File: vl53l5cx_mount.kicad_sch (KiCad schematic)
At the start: 10 parts, among them J1 Conn_01x05_MountingPin, U1 VL53L5CXV0GC/1

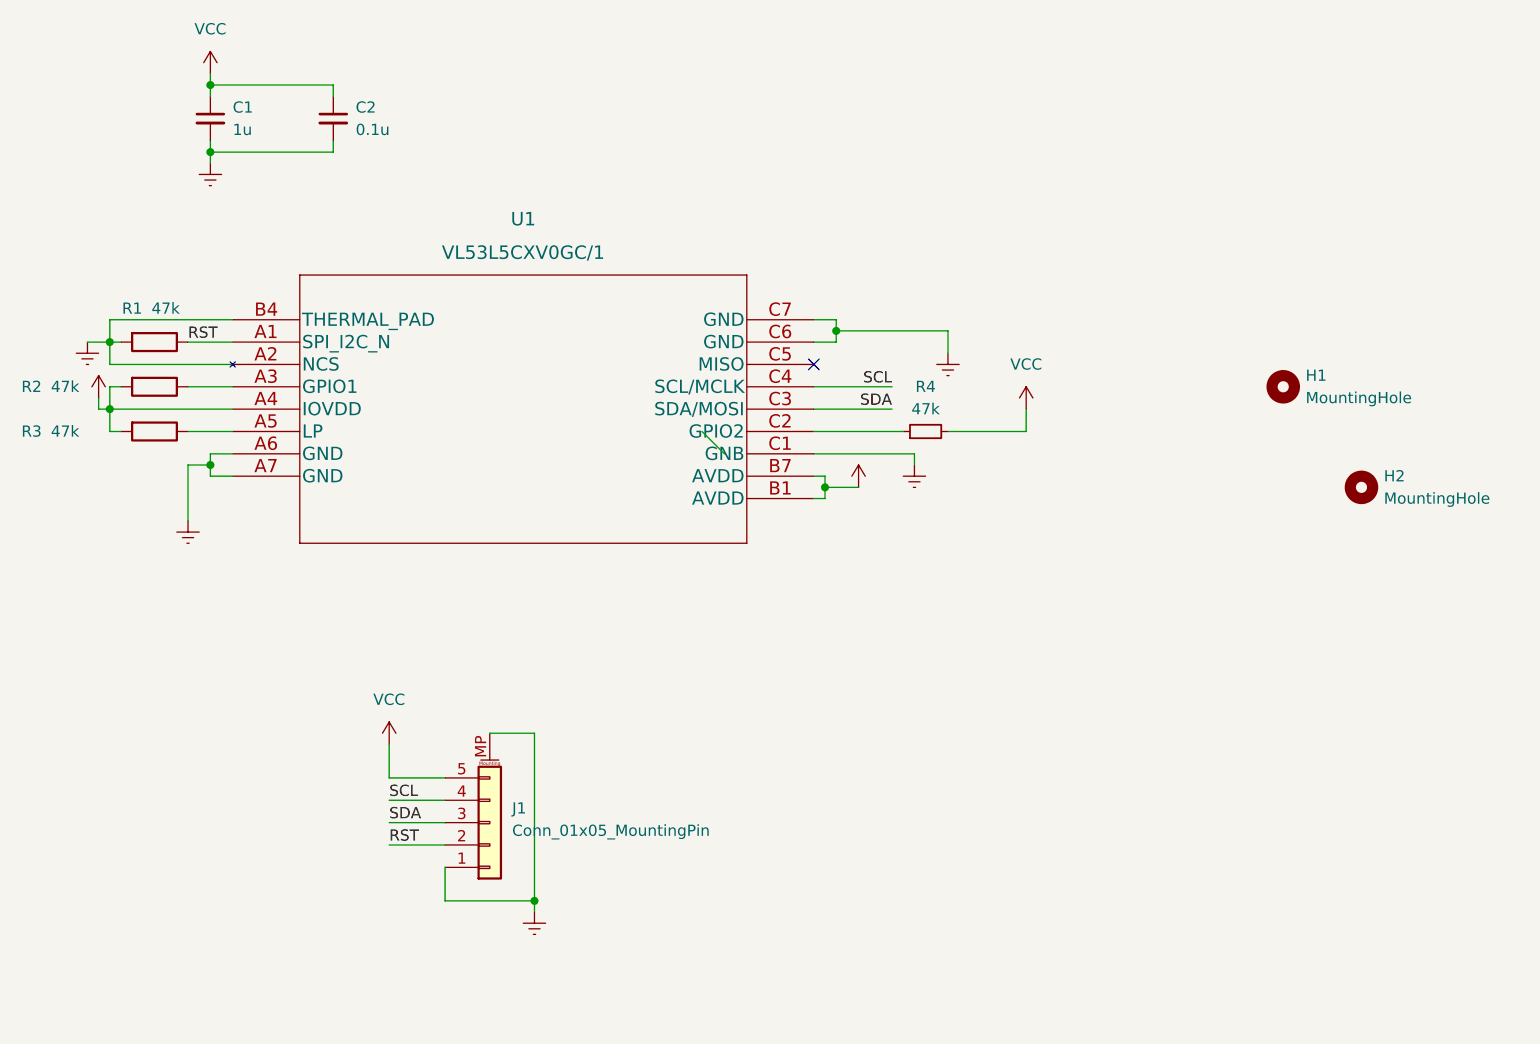
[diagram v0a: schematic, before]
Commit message: reduced component count
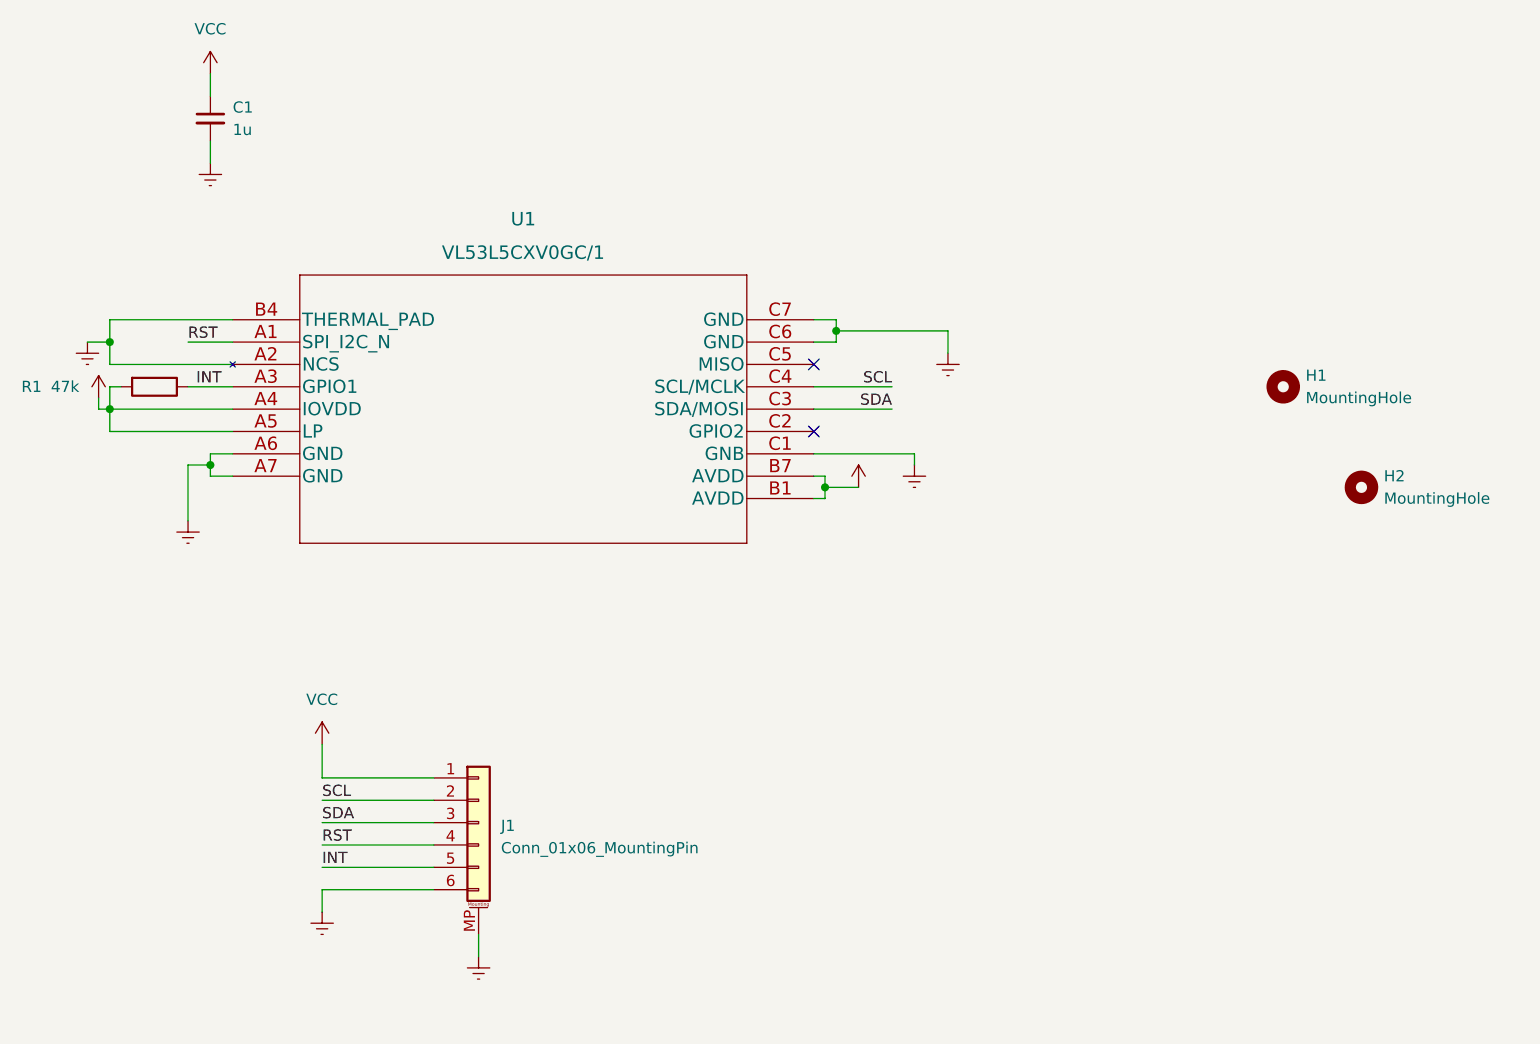
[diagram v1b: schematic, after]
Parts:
- removed C2: 0.1u, Capacitor_SMD:C_0402_1005Metric, symbol Device:C_Small
- removed J1: Conn_01x05_MountingPin, Connector_JST:JST_SH_BM05B-SRSS-TB_1x05-1MP_P1.00mm_Vertical, symbol Connector_Generic_MountingPin:Conn_01x05_MountingPin
- removed R2, R3: 47k, Resistor_SMD:R_0402_1005Metric, symbol Device:R
- removed R4: 47k, Resistor_SMD:R_0402_1005Metric, symbol Device:R_Small
- added J1: Conn_01x06_MountingPin, Connector_JST:JST_SH_BM06B-SRSS-TB_1x06-1MP_P1.00mm_Vertical, symbol Connector_Generic_MountingPin:Conn_01x06_MountingPin
- H1, H2: footprint scew:m1 -> MountingHole:MountingHole_2.2mm_M2_DIN965
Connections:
- net Earth: now also J1.6 (Pin_6), J1.MP (MountPin); no longer R1.2
- net RST: now also J1.4 (Pin_4); no longer R1.1
- net SCL: now also J1.2 (Pin_2)
- net SDA: now also J1.3 (Pin_3)
- net VCC: now also R1.2, U1.A5 (LP), J1.1 (Pin_1)
- net INT: now reaches U1.A3 (GPIO1)
- net INT: now also R1.1, J1.5 (Pin_5)
- no-connect marks 1 -> 2

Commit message: fix connector and edges
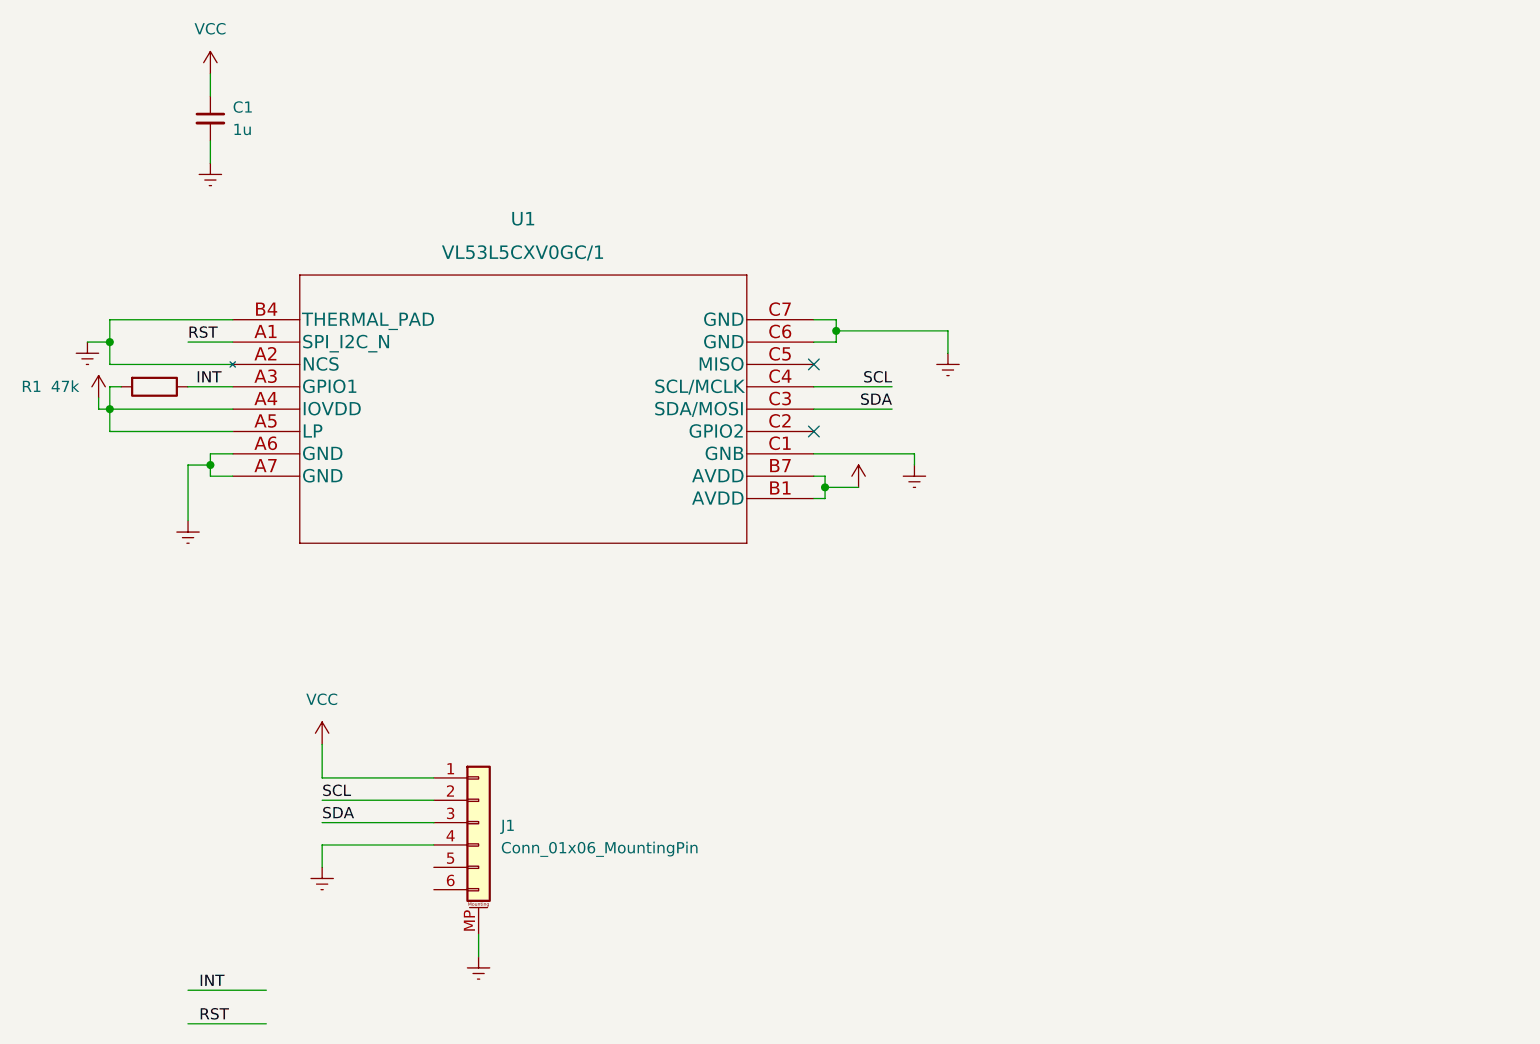
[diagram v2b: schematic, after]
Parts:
- removed H1, H2: MountingHole, MountingHole:MountingHole_2.2mm_M2_DIN965, symbol Mechanical:MountingHole
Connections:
- net Earth: now also J1.4 (Pin_4); no longer J1.6 (Pin_6)
- net INT: no longer J1.5 (Pin_5)
- net RST: no longer J1.4 (Pin_4)
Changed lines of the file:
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@@
     (stroke (width 0) (type default) (color 0 0 0 0))
   )
-  (wire (pts (xy 114.3 139.7) (xy 127 139.7))
+  (wire (pts (xy 99.06 153.67) (xy 107.95 153.67))
     (stroke (width 0) (type default) (color 0 0 0 0))
   )
@@
     (stroke (width 0) (type default) (color 0 0 0 0))
   )
+  (wire (pts (xy 99.06 157.48) (xy 107.95 157.48))
+    (stroke (width 0) (type default) (color 0 0 0 0))
+  )
+  (wire (pts (xy 90.17 77.47) (xy 104.14 77.47))
+    (stroke (width 0) (type default) (color 0 0 0 0))
+  )
+  (wire (pts (xy 171.45 96.52) (xy 175.26 96.52))
+    (stroke (width 0) (type default) (color 0 0 0 0))
+  )
+  (wire (pts (xy 88.9 86.36) (xy 88.9 87.63))
+    (stroke (width 0) (type default) (color 0 0 0 0))
+  )
+  (wire (pts (xy 114.3 137.16) (xy 114.3 139.7))
+    (stroke (width 0) (type default) (color 0 0 0 0))
+  )
+  (wire (pts (xy 114.3 134.62) (xy 127 134.62))
+    (stroke (width 0) (type default) (color 0 0 0 0))
+  )
+  (wire (pts (xy 101.6 93.98) (xy 99.06 93.98))
+    (stroke (width 0) (type default) (color 0 0 0 0))
+  )
+  (wire (pts (xy 170.18 97.79) (xy 171.45 97.79))
+    (stroke (width 0) (type default) (color 0 0 0 0))
+  )
+  (wire (pts (xy 101.6 95.25) (xy 104.14 95.25))
+    (stroke (width 0) (type default) (color 0 0 0 0))
+  )
+  (wire (pts (xy 90.17 85.09) (xy 90.17 87.63))
+    (stroke (width 0) (type default) (color 0 0 0 0))
+  )
+  (wire (pts (xy 127 129.54) (xy 114.3 129.54))
+    (stroke (width 0) (type default) (color 0 0 0 0))
+  )
+  (wire (pts (xy 101.6 93.98) (xy 101.6 95.25))
+    (stroke (width 0) (type default) (color 0 0 0 0))
+  )
+  (wire (pts (xy 171.45 97.79) (xy 171.45 96.52))
+    (stroke (width 0) (type default) (color 0 0 0 0))
+  )
+  (wire (pts (xy 114.3 129.54) (xy 114.3 125.73))
+    (stroke (width 0) (type default) (color 0 0 0 0))
+  )
+  (wire (pts (xy 172.72 80.01) (xy 170.18 80.01))
+    (stroke (width 0) (type default) (color 0 0 0 0))
+  )
+  (wire (pts (xy 185.42 78.74) (xy 185.42 81.28))
+    (stroke (width 0) (type default) (color 0 0 0 0))
+  )
+  (wire (pts (xy 99.06 85.09) (xy 104.14 85.09))
+    (stroke (width 0) (type default) (color 0 0 0 0))
+  )
+  (wire (pts (xy 172.72 78.74) (xy 185.42 78.74))
+    (stroke (width 0) (type default) (color 0 0 0 0))
+  )
+  (wire (pts (xy 170.18 95.25) (xy 171.45 95.25))
+    (stroke (width 0) (type default) (color 0 0 0 0))
+  )
   (wire (pts (xy 114.3 137.16) (xy 127 137.16))
-    (stroke (width 0) (type default) (color 0 0 0 0))
-  )
-  (wire (pts (xy 90.17 77.47) (xy 104.14 77.47))
-    (stroke (width 0) (type default) (color 0 0 0 0))
-  )
-  (wire (pts (xy 171.45 96.52) (xy 175.26 96.52))
-    (stroke (width 0) (type default) (color 0 0 0 0))
-  )
-  (wire (pts (xy 88.9 86.36) (xy 88.9 87.63))
-    (stroke (width 0) (type default) (color 0 0 0 0))
-  )
-  (wire (pts (xy 114.3 142.24) (xy 114.3 144.78))
-    (stroke (width 0) (type default) (color 0 0 0 0))
-  )
-  (wire (pts (xy 114.3 134.62) (xy 127 134.62))
-    (stroke (width 0) (type default) (color 0 0 0 0))
-  )
-  (wire (pts (xy 101.6 93.98) (xy 99.06 93.98))
-    (stroke (width 0) (type default) (color 0 0 0 0))
-  )
-  (wire (pts (xy 170.18 97.79) (xy 171.45 97.79))
-    (stroke (width 0) (type default) (color 0 0 0 0))
-  )
-  (wire (pts (xy 101.6 95.25) (xy 104.14 95.25))
-    (stroke (width 0) (type default) (color 0 0 0 0))
-  )
-  (wire (pts (xy 90.17 85.09) (xy 90.17 87.63))
-    (stroke (width 0) (type default) (color 0 0 0 0))
-  )
-  (wire (pts (xy 127 129.54) (xy 114.3 129.54))
-    (stroke (width 0) (type default) (color 0 0 0 0))
-  )
-  (wire (pts (xy 101.6 93.98) (xy 101.6 95.25))
-    (stroke (width 0) (type default) (color 0 0 0 0))
-  )
-  (wire (pts (xy 171.45 97.79) (xy 171.45 96.52))
-    (stroke (width 0) (type default) (color 0 0 0 0))
-  )
-  (wire (pts (xy 114.3 129.54) (xy 114.3 125.73))
-    (stroke (width 0) (type default) (color 0 0 0 0))
-  )
-  (wire (pts (xy 172.72 80.01) (xy 170.18 80.01))
-    (stroke (width 0) (type default) (color 0 0 0 0))
-  )
-  (wire (pts (xy 185.42 78.74) (xy 185.42 81.28))
-    (stroke (width 0) (type default) (color 0 0 0 0))
-  )
-  (wire (pts (xy 99.06 85.09) (xy 104.14 85.09))
-    (stroke (width 0) (type default) (color 0 0 0 0))
-  )
-  (wire (pts (xy 172.72 78.74) (xy 185.42 78.74))
-    (stroke (width 0) (type default) (color 0 0 0 0))
-  )
-  (wire (pts (xy 170.18 95.25) (xy 171.45 95.25))
-    (stroke (width 0) (type default) (color 0 0 0 0))
-  )
-  (wire (pts (xy 114.3 142.24) (xy 127 142.24))
     (stroke (width 0) (type default) (color 0 0 0 0))
   )
@@
     (effects (font (size 1.27 1.27)) (justify left bottom))
   )
-  (label "RST" (at 114.3 137.16 0)
+  (label "RST" (at 100.33 157.48 0)
     (effects (font (size 1.27 1.27)) (justify left bottom))
   )
@@
     (effects (font (size 1.27 1.27)) (justify right bottom))
   )
-  (label "INT" (at 114.3 139.7 0)
+  (label "INT" (at 100.33 153.67 0)
     (effects (font (size 1.27 1.27)) (justify left bottom))
   )
@@
     )
     (pin "1")
-  )
-  (symbol (lib_id "Mechanical:MountingHole") (at 223.52 85.09 0) (unit 1)
-    (in_bom yes) (on_board yes) (fields_autoplaced)
-    (property "Reference" "H1" (id 0) (at 226.06 83.8199 0)
-      (effects (font (size 1.27 1.27)) (justify left))
-    )
-    (property "Value" "MountingHole" (id 1) (at 226.06 86.3599 0)
-      (effects (font (size 1.27 1.27)) (justify left))
-    )
-    (property "Footprint" "MountingHole:MountingHole_2.2mm_M2_DIN965" (id 2) (at 223.52 85.09 0)
-      (effects (font (size 1.27 1.27)) hide)
-    )
-    (property "Datasheet" "~" (id 3) (at 223.52 85.09 0)
-      (effects (font (size 1.27 1.27)) hide)
-    )
   )
   (symbol (lib_id "power:Earth") (at 132.08 149.86 0) (unit 1)
@@
     (pin "1")
   )
-  (symbol (lib_id "power:Earth") (at 114.3 144.78 0) (unit 1)
-    (in_bom yes) (on_board yes) (fields_autoplaced)
-    (property "Reference" "#PWR0108" (id 0) (at 114.3 151.13 0)
-      (effects (font (size 1.27 1.27)) hide)
-    )
-    (property "Value" "Earth" (id 1) (at 114.3 148.59 0)
-      (effects (font (size 1.27 1.27)) hide)
-    )
-    (property "Footprint" "" (id 2) (at 114.3 144.78 0)
-      (effects (font (size 1.27 1.27)) hide)
-    )
-    (property "Datasheet" "~" (id 3) (at 114.3 144.78 0)
+  (symbol (lib_id "power:Earth") (at 114.3 139.7 0) (unit 1)
+    (in_bom yes) (on_board yes) (fields_autoplaced)
+    (property "Reference" "#PWR0108" (id 0) (at 114.3 146.05 0)
+      (effects (font (size 1.27 1.27)) hide)
+    )
+    (property "Value" "Earth" (id 1) (at 114.3 143.51 0)
+      (effects (font (size 1.27 1.27)) hide)
+    )
+    (property "Footprint" "" (id 2) (at 114.3 139.7 0)
+      (effects (font (size 1.27 1.27)) hide)
+    )
+    (property "Datasheet" "~" (id 3) (at 114.3 139.7 0)
       (effects (font (size 1.27 1.27)) hide)
     )
@@
     (pin "1")
   )
-  (symbol (lib_id "Mechanical:MountingHole") (at 232.41 96.52 0) (unit 1)
-    (in_bom yes) (on_board yes) (fields_autoplaced)
-    (property "Reference" "H2" (id 0) (at 234.95 95.2499 0)
-      (effects (font (size 1.27 1.27)) (justify left))
-    )
-    (property "Value" "MountingHole" (id 1) (at 234.95 97.7899 0)
-      (effects (font (size 1.27 1.27)) (justify left))
-    )
-    (property "Footprint" "MountingHole:MountingHole_2.2mm_M2_DIN965" (id 2) (at 232.41 96.52 0)
-      (effects (font (size 1.27 1.27)) hide)
-    )
-    (property "Datasheet" "~" (id 3) (at 232.41 96.52 0)
-      (effects (font (size 1.27 1.27)) hide)
-    )
-  )
   (symbol (lib_id "Device:R") (at 95.25 85.09 270) (unit 1)
     (in_bom yes) (on_board yes)
@@
       (reference "C1") (unit 1) (value "1u") (footprint "Capacitor_SMD:C_0402_1005Metric")
     )
-    (path "/34cf2a06-8146-4463-b074-bb240ce4dd21"
-      (reference "H1") (unit 1) (value "MountingHole") (footprint "MountingHole:MountingHole_2.2mm_M2_DIN965")
-    )
-    (path "/cb1463e1-4818-4985-acab-6c383f1e53a1"
-      (reference "H2") (unit 1) (value "MountingHole") (footprint "MountingHole:MountingHole_2.2mm_M2_DIN965")
-    )
     (path "/47be24ee-e15b-4cee-b84b-350111ac1499"

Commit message: update silkscreen
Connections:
- net INT: now also J1.6 (Pin_6)
- net RST: now also J1.5 (Pin_5)
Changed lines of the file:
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@@
     (stroke (width 0) (type default) (color 0 0 0 0))
   )
-  (wire (pts (xy 99.06 153.67) (xy 107.95 153.67))
+  (wire (pts (xy 118.11 142.24) (xy 127 142.24))
     (stroke (width 0) (type default) (color 0 0 0 0))
   )
@@
     (stroke (width 0) (type default) (color 0 0 0 0))
   )
-  (wire (pts (xy 99.06 157.48) (xy 107.95 157.48))
+  (wire (pts (xy 118.11 139.7) (xy 127 139.7))
     (stroke (width 0) (type default) (color 0 0 0 0))
   )
@@
     (effects (font (size 1.27 1.27)) (justify left bottom))
   )
-  (label "RST" (at 100.33 157.48 0)
+  (label "RST" (at 118.11 139.7 0)
     (effects (font (size 1.27 1.27)) (justify left bottom))
   )
@@
     (effects (font (size 1.27 1.27)) (justify right bottom))
   )
-  (label "INT" (at 100.33 153.67 0)
+  (label "INT" (at 118.11 142.24 0)
     (effects (font (size 1.27 1.27)) (justify left bottom))
   )
